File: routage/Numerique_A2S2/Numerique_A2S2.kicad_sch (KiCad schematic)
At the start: 7 parts, among them J1 Conn_01x06_Pin, U1 PIC16F877A-IP, U2 LM7805_TO220, Y1 Crystal

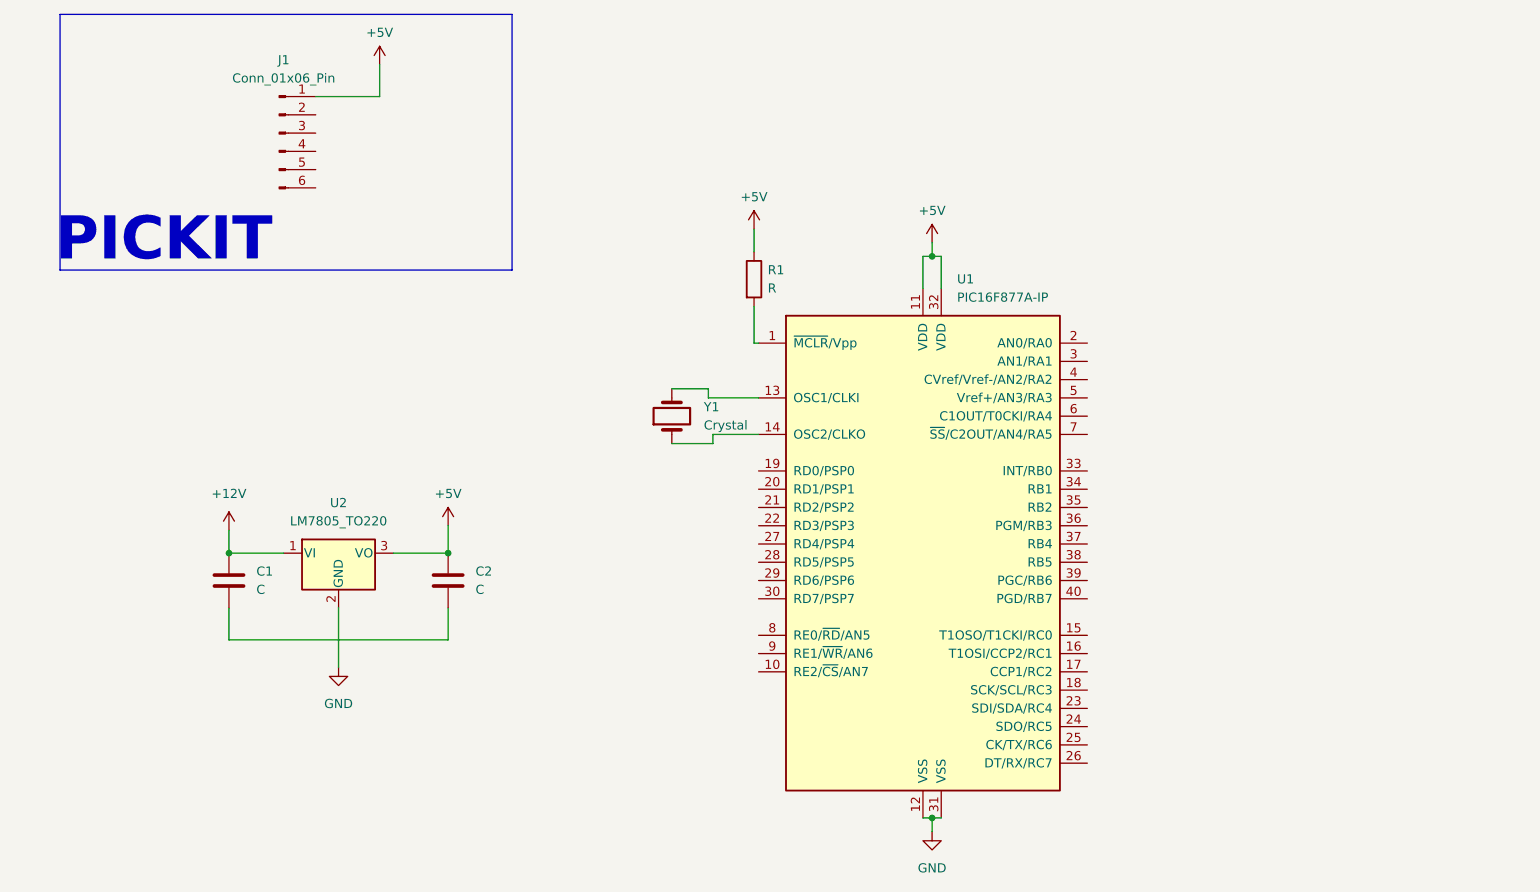
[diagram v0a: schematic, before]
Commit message: Modification du routage ajout de la regulation changement uC et integration Potar pour test CAN
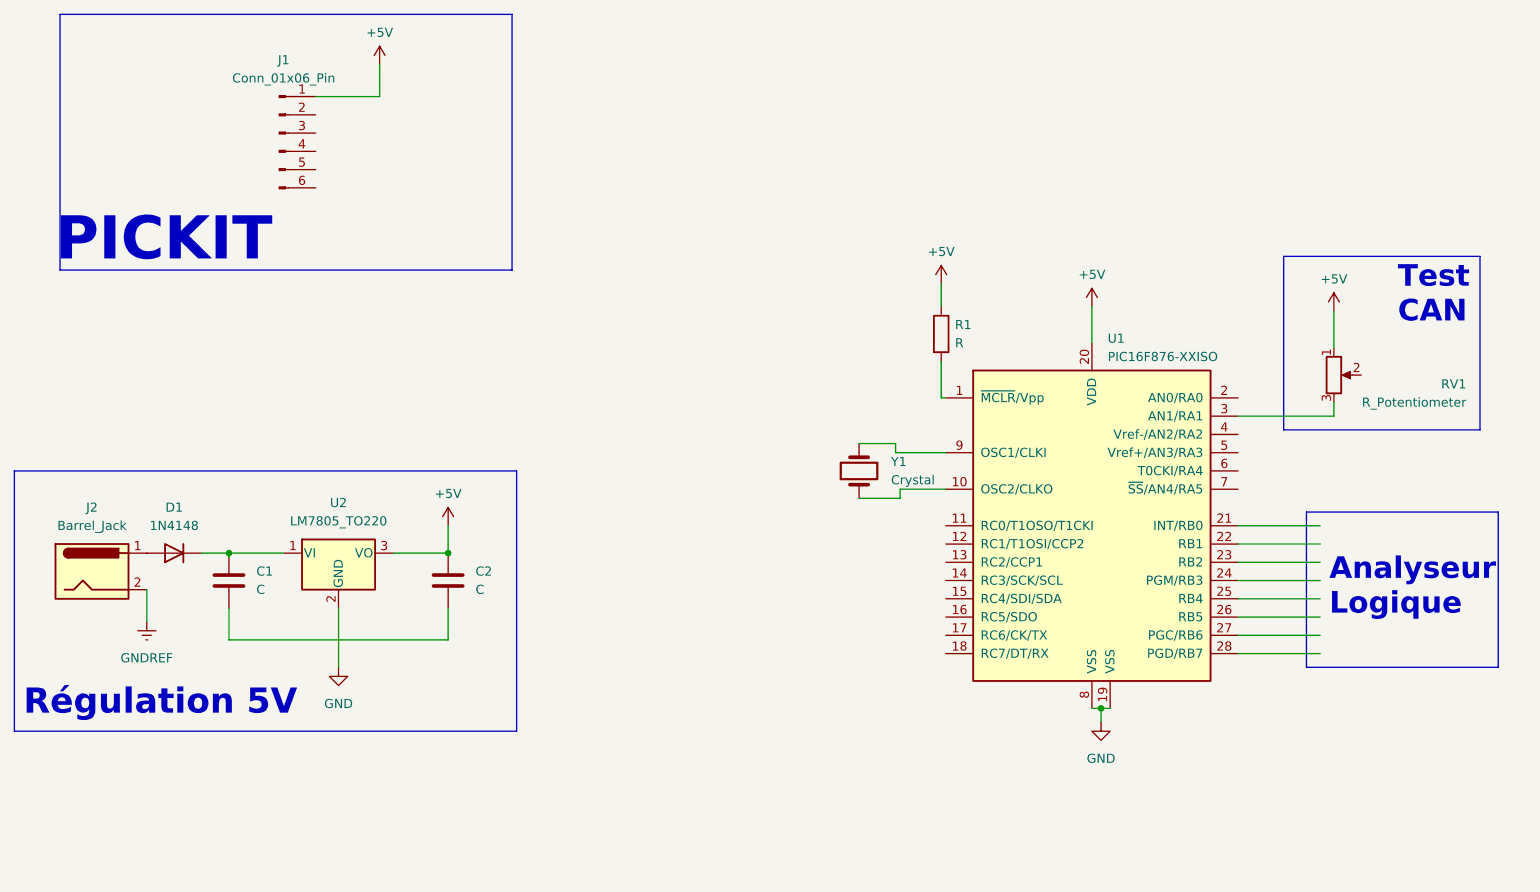
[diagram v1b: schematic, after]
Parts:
- removed U1: PIC16F877A-IP, symbol MCU_Microchip_PIC16:PIC16F877A-IP
- added D1: 1N4148, Diode_THT:D_DO-35_SOD27_P7.62mm_Horizontal, symbol Diode:1N4148
- added J2: Barrel_Jack, symbol Connector:Barrel_Jack
- added RV1: R_Potentiometer, symbol Device:R_Potentiometer
- added U1: PIC16F876-XXISO, symbol MCU_Microchip_PIC16:PIC16F876-XXISO
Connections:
- net +5V: now also RV1.1, U1.20 (VDD)
- net GND: now also U1.19 (VSS), U1.8 (VSS)
- net at Y1.1: now also U1.10 (OSC2/CLKO)
- net at Y1.2: now also U1.9 (OSC1/CLKI)
- net at R1.2: now also U1.1 (~{MCLR}/Vpp)
- net +12V: no longer names the net of C1.1, U2.1 (VI)
- net +12V: now also D1.1 (K)
- new net: D1.2 (A), J2.1
- new net: RV1.3, U1.3 (AN1/RA1)
- new net GNDREF: J2.2
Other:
- note added: "Analyseur Logique"
- note added: "Régulation 5V"
- note added: "Test CAN"
- moved on the sheet: R1, Y1

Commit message: Ajout de la partie régulation et condos sur le quartz
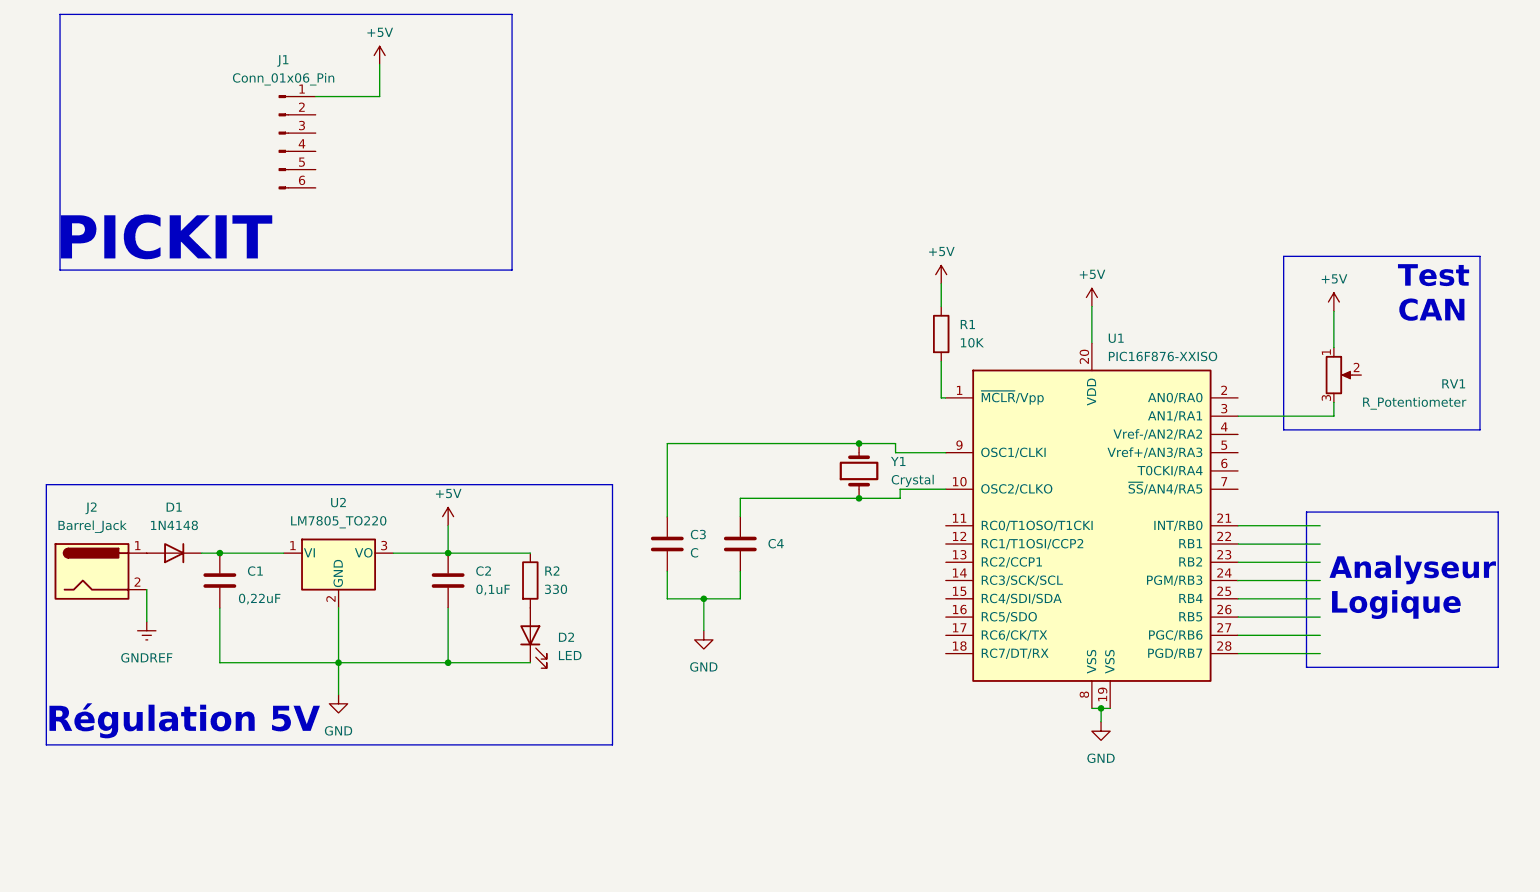
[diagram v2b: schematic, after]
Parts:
- added C3: C, symbol Device:C
- added C4: ~, symbol Device:C
- added D2: LED, symbol Device:LED
- added R2: 330, symbol Device:R
- C1: value C -> 0,22uF
- C2: value C -> 0,1uF
- R1: value R -> 10K
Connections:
- net +5V: now also R2.1
- net GND: now also C1.2, C2.2, C3.2, C4.2, D2.1 (K)
- net at U1.10 (OSC2/CLKO), Y1.1: now also C4.1
- net at U1.9 (OSC1/CLKI), Y1.2: now also C3.1
- new net: D2.2 (A), R2.2
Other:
- moved on the sheet: C1

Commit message: Modification du schema ajout de plusieurs feuille pour schematiser le projet dans ces différentes phase
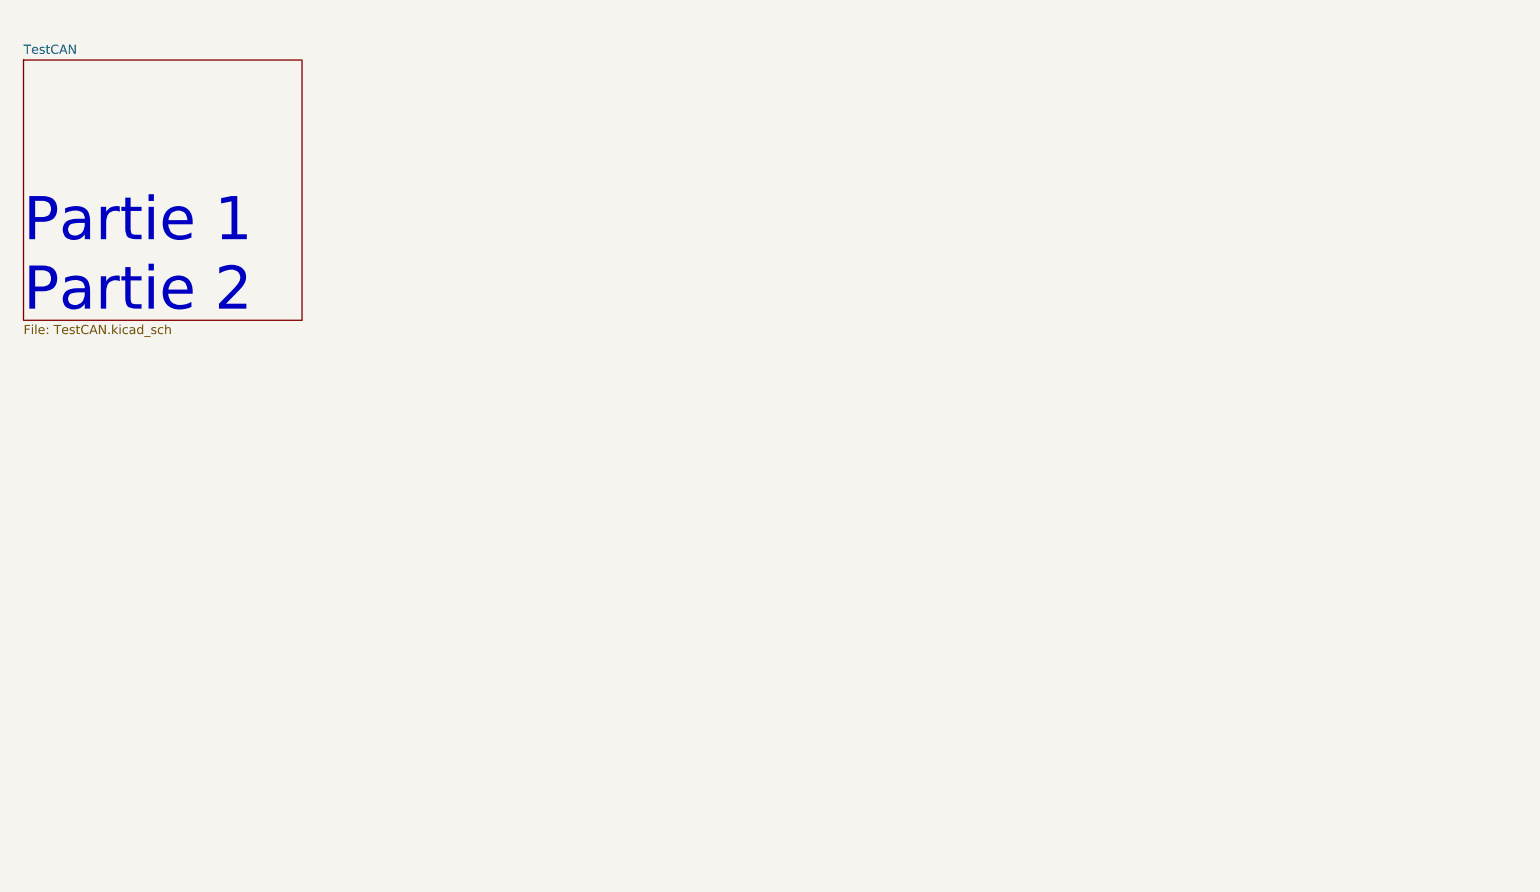
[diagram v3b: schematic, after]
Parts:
- removed C1: 0,22uF, symbol Device:C
- removed C2: 0,1uF, symbol Device:C
- removed C3: C, symbol Device:C
- removed C4: ~, symbol Device:C
- removed D1: 1N4148, Diode_THT:D_DO-35_SOD27_P7.62mm_Horizontal, symbol Diode:1N4148
- removed D2: LED, symbol Device:LED
- removed J1: Conn_01x06_Pin, symbol Connector:Conn_01x06_Pin
- removed J2: Barrel_Jack, symbol Connector:Barrel_Jack
- removed R1: 10K, symbol Device:R
- removed R2: 330, symbol Device:R
- removed RV1: R_Potentiometer, symbol Device:R_Potentiometer
- removed U1: PIC16F876-XXISO, symbol MCU_Microchip_PIC16:PIC16F876-XXISO
- removed U2: LM7805_TO220, Package_TO_SOT_THT:TO-220-3_Vertical, symbol Regulator_Linear:LM7805_TO220
- removed Y1: Crystal, symbol Device:Crystal
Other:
- added sheet TestCAN (TestCAN.kicad_sch)
- note added: "Partie 1 Partie 2"
- note removed: "Analyseur Logique"
- note removed: "PICKIT"
- note removed: "Régulation 5V"
- note removed: "Test CAN"

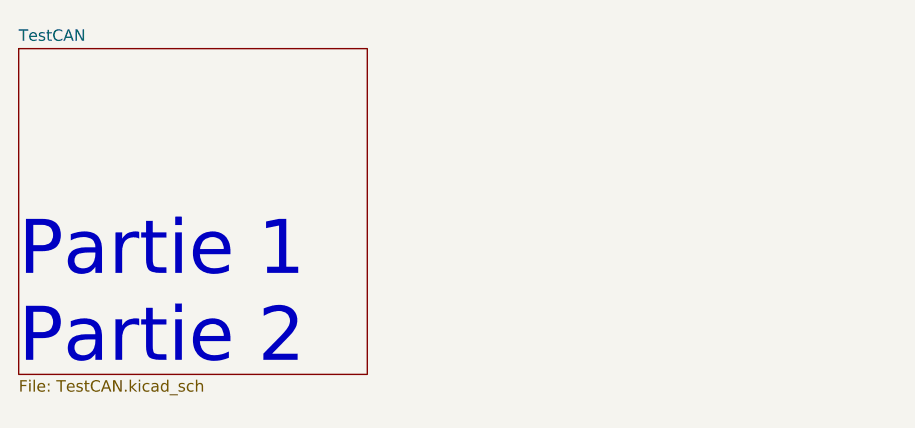
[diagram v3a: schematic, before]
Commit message: Creation dune lib pour le decoder LCD et creation d un schema pour la partie 4
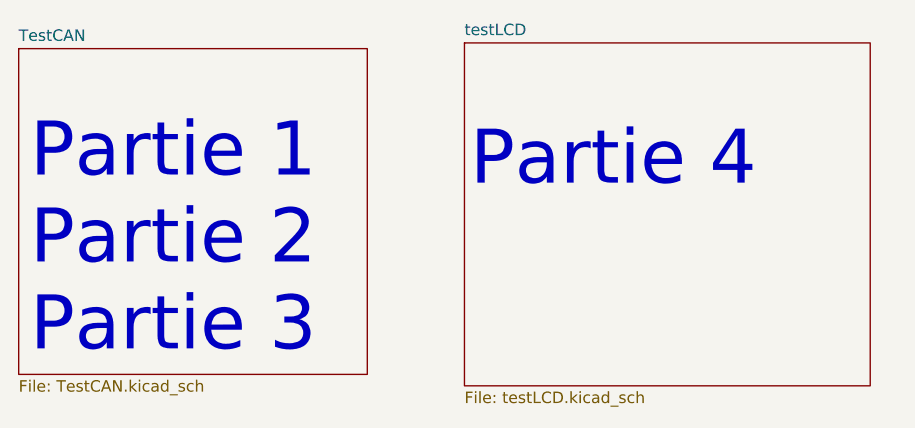
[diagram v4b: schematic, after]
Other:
- added sheet testLCD (testLCD.kicad_sch)
- note added: "Partie 1 Partie 2 Partie 3"
- note added: "Partie 4"
- note removed: "Partie 1 Partie 2"
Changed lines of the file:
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@@
     (comment 2 "Membres : RAFFOUX JOIRE ANDRIANJAFINDRADILO")
   )
-  (text "Partie 1\nPartie 2" (at 34.925 62.865 0)
+  (text "Partie 1\nPartie 2\nPartie 3" (at 36.195 61.595 0)
+    (effects (font (size 6 6)) (justify left bottom))
+  )
+  (text "Partie 4" (at 85.09 43.18 0)
     (effects (font (size 6 6)) (justify left bottom))
   )
@@
       )
     )
+  )
+  (sheet (at 84.455 26.67) (size 45.085 38.1) (fields_autoplaced)
+    (stroke (width 0.1524) (type solid))
+    (fill (color 0 0 0 0.0000))
+    (property "Sheetname" "testLCD" (at 84.455 25.9584 0)
+      (effects (font (size 1.27 1.27)) (justify left bottom))
+    )
+    (property "Sheetfile" "testLCD.kicad_sch" (at 84.455 65.3546 0)
+      (effects (font (size 1.27 1.27)) (justify left top))
+    )
+    (instances
+      (project "Numerique_A2S2"
+        (path "/c9018090-be6b-47c3-acdf-7658c7cb0715" (page "3"))
+      )
+    )

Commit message: Modification condo
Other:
- note added: "Partie 4 Partie 5 Partie 6"
- note removed: "Partie 4"
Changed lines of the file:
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@@
     (effects (font (size 6 6)) (justify left bottom))
   )
-  (text "Partie 4" (at 85.09 43.18 0)
+  (text "Partie 4\nPartie 5\nPartie 6" (at 86.36 57.15 0)
     (effects (font (size 6 6)) (justify left bottom))
   )
